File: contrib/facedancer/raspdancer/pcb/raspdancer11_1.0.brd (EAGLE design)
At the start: 25.8 x 33.3 mm, 15 parts, among them Q1 12Mhz

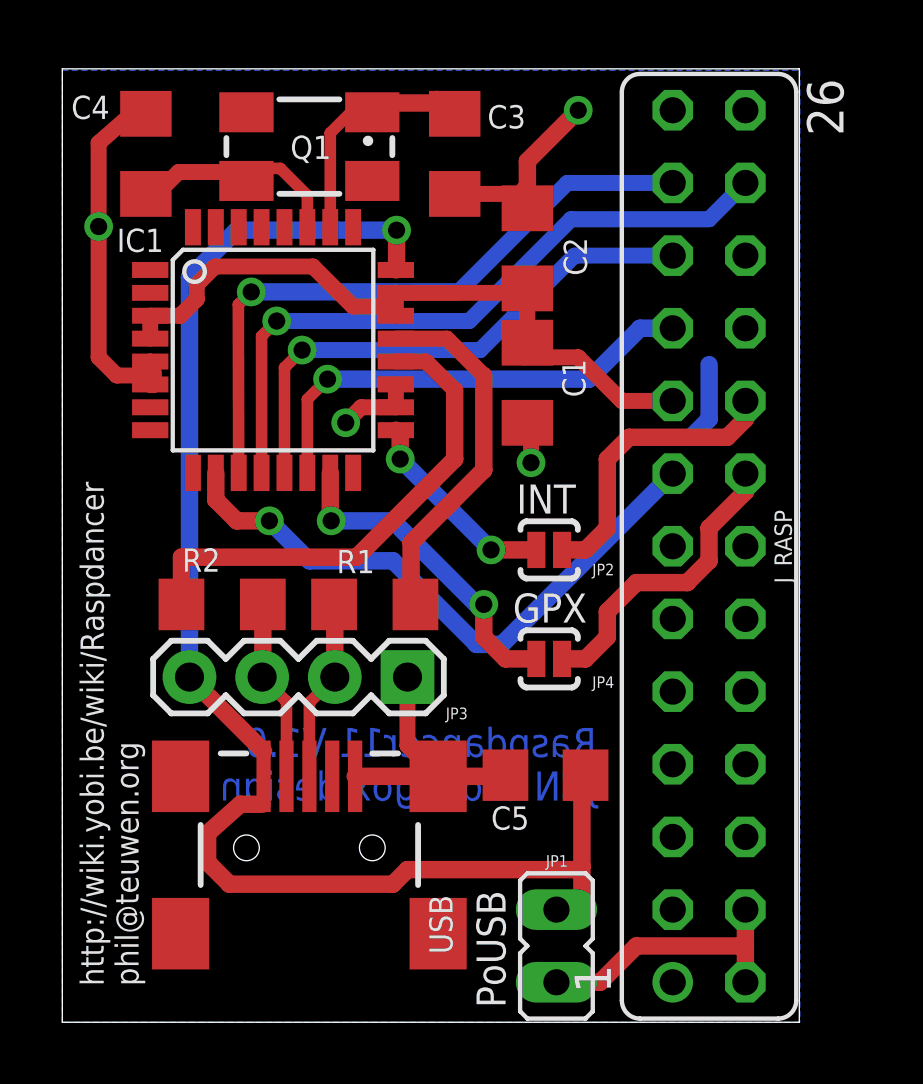
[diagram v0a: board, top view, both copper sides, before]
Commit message: raspdancer11 board: more room around IC and other small changes
git-svn-id: https://svn.code.sf.net/p/goodfet/code@1586 12e2690d-a6be-4b82-a7b7-67c4a43b65c8
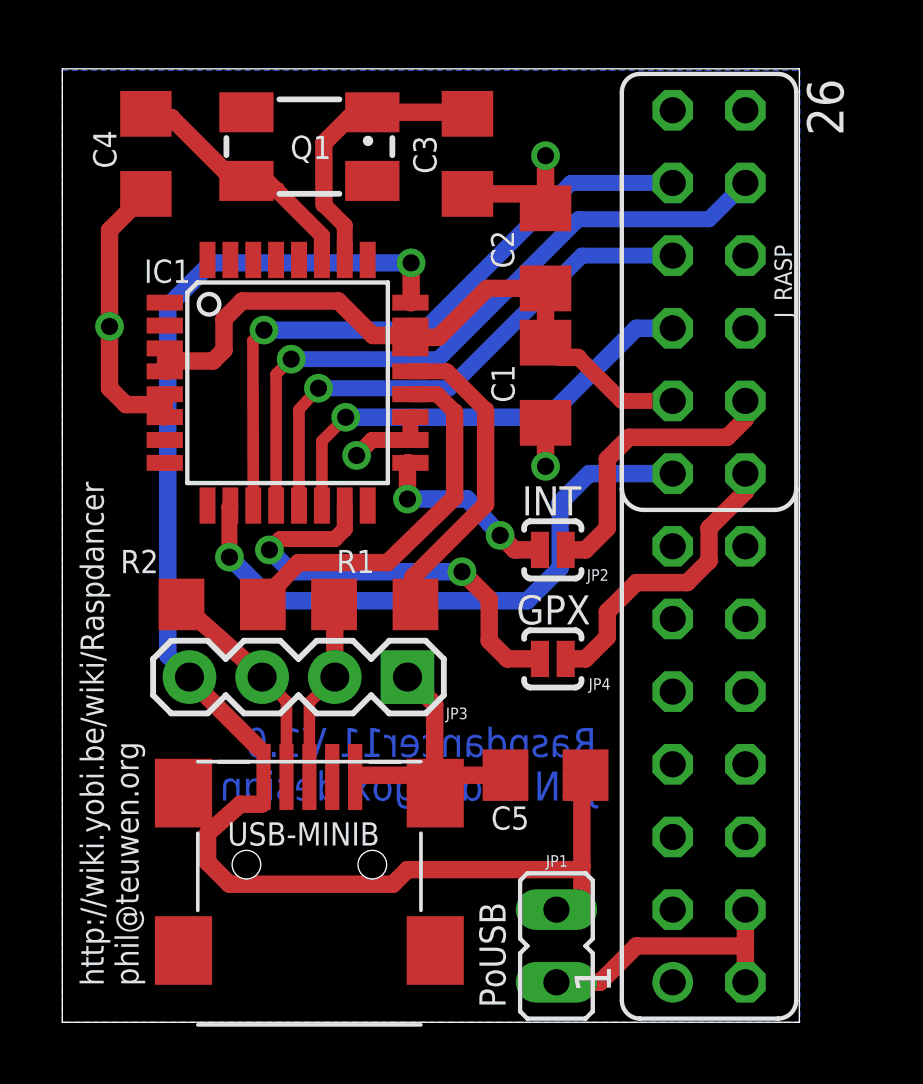
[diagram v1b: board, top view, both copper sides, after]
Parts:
- removed USB: USB-MINIB-5PIN, SparkFun:USB-MINIB
- added USB-MINIB: (no value), adafruit:USB-MINIB
- moved IC1 1.25 mm to (7.87, 22.4)
- moved C1 0.63 mm to (16.9, 22.4)
- moved C2 0.63 mm to (16.9, 27.1)
- moved C3 0.44 mm to (14.2, 30.4)
- moved JP2 0.13 mm to (17.1, 16.5)
- moved JP4 0.13 mm to (17.1, 12.7)
- turned C4 to 270 degrees
- turned R2 to 0 degrees
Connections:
- net N$1 renamed D+
- net N$10 renamed GPX2
- net N$11 renamed GPX
- net N$13 renamed VBUS2
- net N$2 renamed IX
- net N$3 renamed XO
- net N$7 renamed D-
- net N$9 renamed INT2
- removed net N$4: C5.2, IC1.24, JP1.1, JP3.4, USB.VBUS
- removed net N$5: JP3.2, R1.1, USB.D+
- removed net N$6: JP3.3, R2.1, USB.D-
- new net D+2: JP3.2, R1.1, USB-MINIB.D+
- new net D-2: JP3.3, R2.1, USB-MINIB.D-
- new net VBUS: C5.2, IC1.24, JP1.1, JP3.4, USB-MINIB.VBUS
- net GND: now also USB-MINIB.GND; no longer USB.GND, USB.MTN4
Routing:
- net N$4: track 51.2 -> 0.00 mm, vias 1 -> 0
- net VBUS: track 0.00 -> 50.0 mm, vias 0 -> 1
- net D-2: track 0.00 -> 7.70 mm
- net GND: track 37.0 -> 29.7 mm
- net N$5: track 7.09 -> 0.00 mm
- net N$6: track 6.40 -> 0.00 mm
- net D+2: track 0.00 -> 6.35 mm
- net GPX: track 11.5 -> 15.6 mm
- net D-: track 17.5 -> 13.6 mm
- net XO: track 8.69 -> 10.7 mm
- net IX: track 8.74 -> 10.4 mm
- net D+: track 12.7 -> 11.1 mm
- net VBUS2: track 9.54 -> 10.2 mm
